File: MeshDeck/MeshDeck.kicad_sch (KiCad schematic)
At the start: 25 parts, among them CN1 ATGM336H-6N-74, SW1 4*4*1.7, SW2 4*4*1.7, U1 ESP32-S3-WROOM-1U-N16R8, U2 SX1262S8S+T-X1, U5 RN32768114

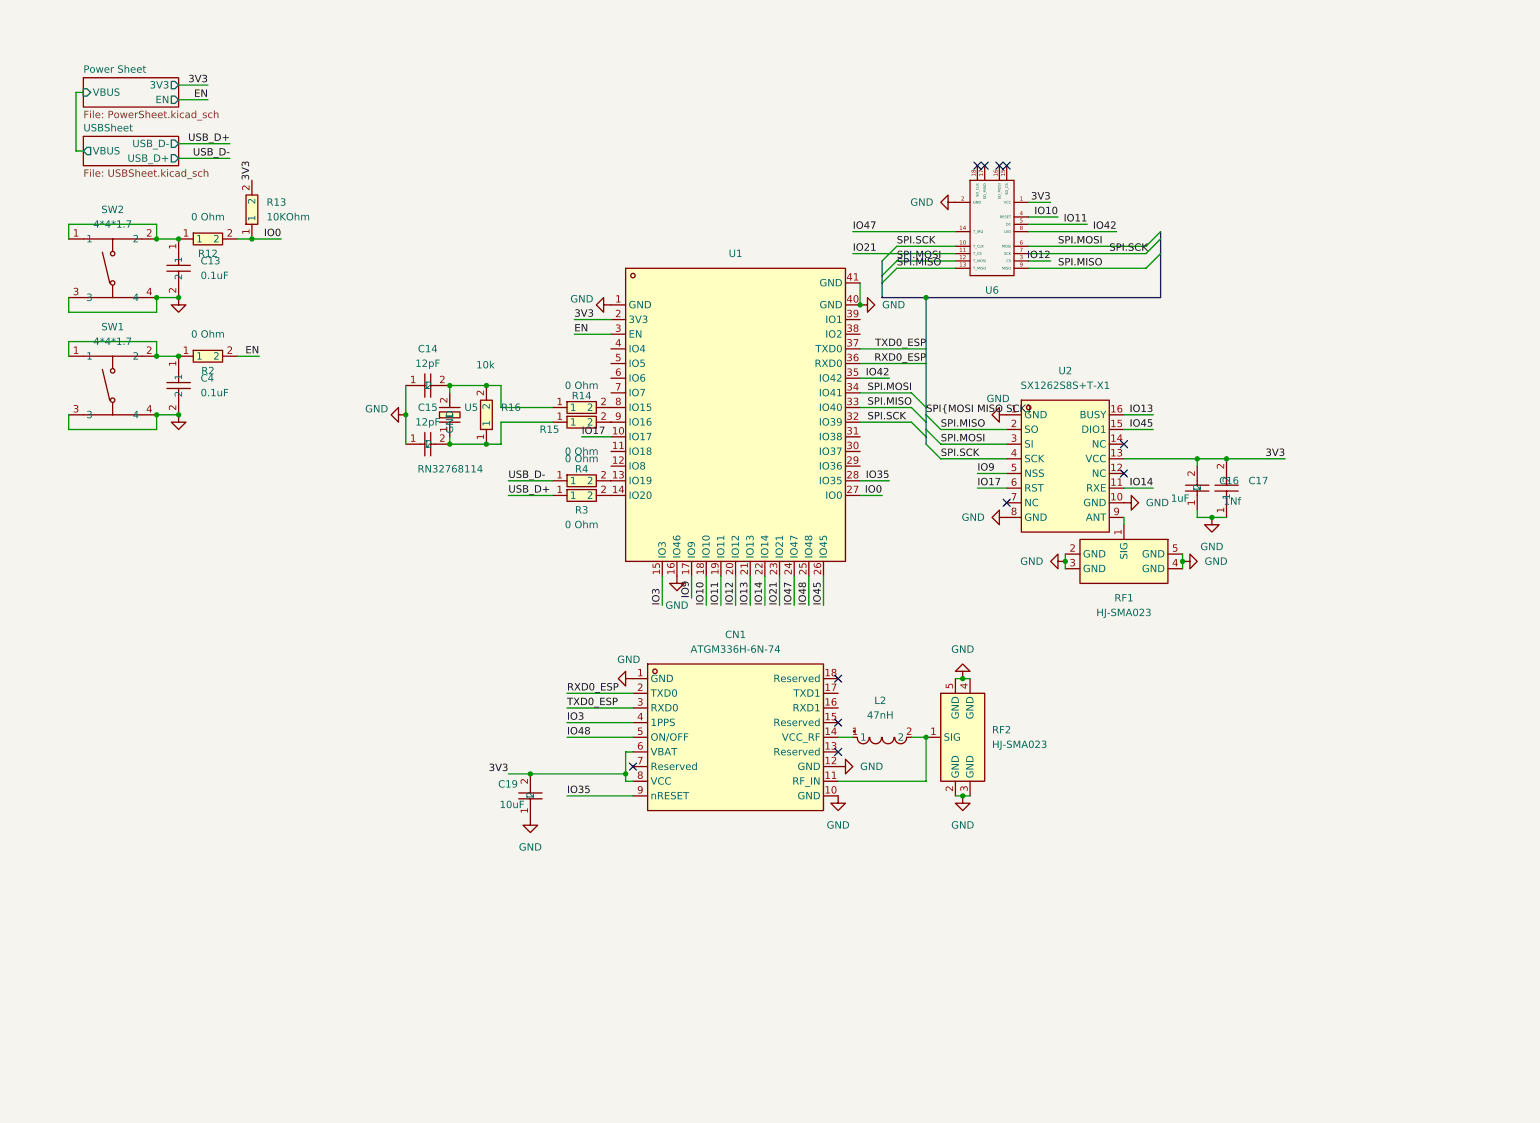
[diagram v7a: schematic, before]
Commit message: added sd card and started keyboard
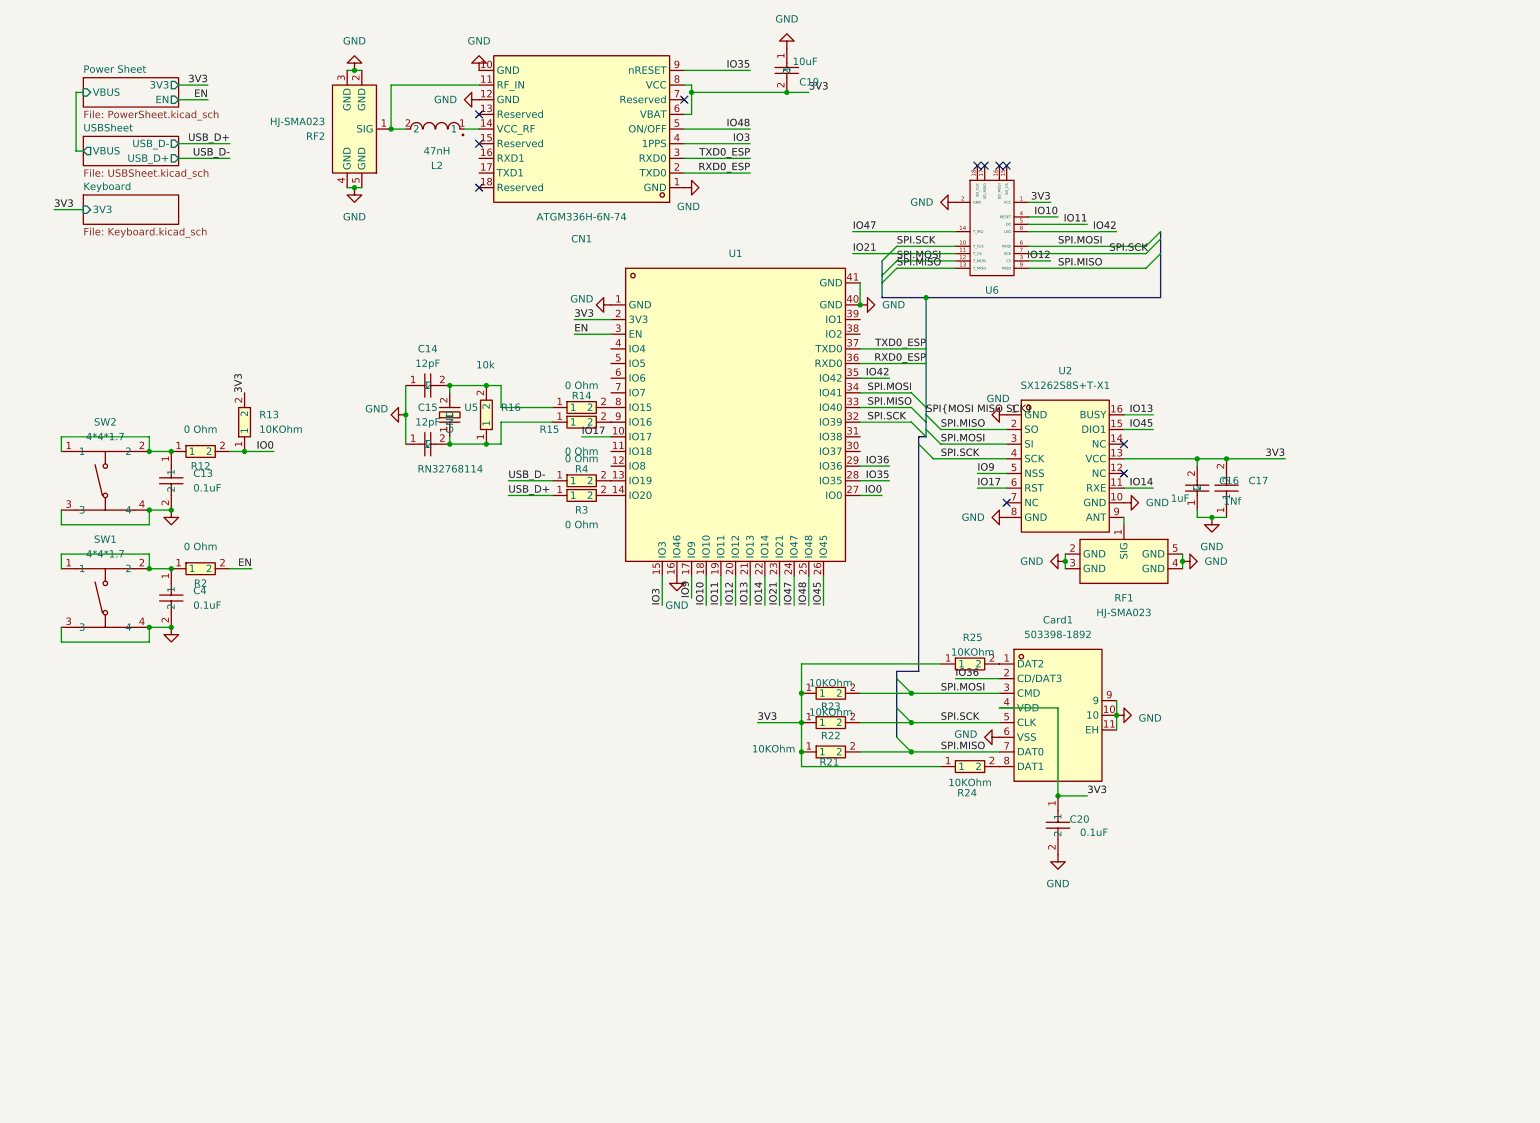
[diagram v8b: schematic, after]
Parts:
- added C20: 0.1uF, MeshDeck:C0402, symbol MeshDeck:CL05B104KO5NNNC
- added Card1: 503398-1892, MeshDeck:TF-SMD_503398-1892, symbol MeshDeck:503398-1892
- added R21, R22, R23, R24, R25: 10KOhm, MeshDeck:R0402, symbol MeshDeck:QR0402F1KQ10
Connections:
- net 3V3: now also C20.1, Card1.4 (VDD), R21.1, R22.1, R23.1, R24.1, R25.1
- net GND: now also C20.2, Card1.10, Card1.11 (EH), Card1.6 (VSS), Card1.9
- net SPI.MISO: now also Card1.7 (DAT0), R21.2
- net SPI.MOSI: now also Card1.3 (CMD), R23.2
- net SPI.SCK: now also Card1.5 (CLK), R22.2
- net IO36: now reaches U1.29 (IO36)
- net IO36: now also Card1.2 (CD/DAT3)
- new net: Card1.1 (DAT2), R25.2
- new net: Card1.8 (DAT1), R24.2
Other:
- added sheet Keyboard (Keyboard.kicad_sch)
- moved on the sheet: C13, C19, C4, CN1, L2, R12, R13, R2, RF2, SW1, SW2
